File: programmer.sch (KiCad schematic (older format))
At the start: 2 parts

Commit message: FPGA change and new project file
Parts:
- removed U?: XC6SLX9-2TQG144I, symbol FPGA_Xilinx_Spartan6:XC6SLX4-TQG144
- added U?: XC7S6-1FTGB196C, Xilinx-XC7S6-1FTGB196C-0-0-*, symbol sdr:XC7S6-1FTGB196C
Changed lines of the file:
@@
 $EndDescr
-$Comp
-L FPGA_Xilinx_Spartan6:XC6SLX4-TQG144 U?
-U 3 1 60050A88
-P 7800 5150
-F 0 "U?" H 6520 5241 50  0000 R CNN
-F 1 "XC6SLX9-2TQG144I" H 6520 5150 50  0000 R CNN
-F 2 "" H 7800 5150 50  0001 C CNN
-F 3 "http://www.farnell.com/datasheets/1763510.pdf" H 6520 5059 50  0000 R CNN
-	3    7800 5150
-	-1   0    0    -1
-$EndComp
 $Comp
 L Interface_USB:FT2232HL U?
@@
 	1    0    0    -1
 $EndComp
+$Comp
+L sdr:XC7S6-1FTGB196C U?
+U 1 1 6004AE97
+P 7450 4000
+F 0 "U?" H 8550 4265 50  0000 C CNN
+F 1 "XC7S6-1FTGB196C" H 8550 4174 50  0000 C CNN
+F 2 "Xilinx-XC7S6-1FTGB196C-0-0-*" H 7450 4400 50  0001 L CNN
+F 3 "https://www.xilinx.com/support/documentation/data_sheets/ds189-spartan-7-data-sheet.pdf" H 7450 4500 50  0001 L CNN
+F 4 "180Kbits" H 7450 4600 50  0001 L CNN "RAM size"
+F 5 "No" H 7450 4700 50  0001 L CNN "automotive"
+F 6 "IC" H 7450 4800 50  0001 L CNN "category"
+F 7 "Integrated Circuits (ICs)" H 7450 4900 50  0001 L CNN "device class L1"
+F 8 "Embedded Processors and Controllers" H 7450 5000 50  0001 L CNN "device class L2"
+F 9 "FPGAs - Field Programmable Gate Arrays" H 7450 5100 50  0001 L CNN "device class L3"
+F 10 "XC7S6-1FTGB196C" H 7450 5200 50  0001 L CNN "digikey description"
+F 11 "122-2240-ND" H 7450 5300 50  0001 L CNN "digikey part number"
+F 12 "https://www.xilinx.com/support/documentation/user_guides/ug475_7Series_Pkg_Pinout.pdf" H 7450 5400 50  0001 L CNN "footprint url"
+F 13 "200MHz" H 7450 5500 50  0001 L CNN "frequency"
+F 14 "1.55mm" H 7450 5600 50  0001 L CNN "height"
+F 15 "BGA196C100P14X14_1500X1500X146" H 7450 5700 50  0001 L CNN "ipc land pattern name"
+F 16 "Yes" H 7450 5800 50  0001 L CNN "lead free"
+F 17 "d5f555df3775b1ed" H 7450 5900 50  0001 L CNN "library id"
+F 18 "Xilinx" H 7450 6000 50  0001 L CNN "manufacturer"
+F 19 "+85°C" H 7450 6100 50  0001 L CNN "max junction temp"
+F 20 "3.465V" H 7450 6200 50  0001 L CNN "max supply voltage"
+F 21 "0.95V" H 7450 6300 50  0001 L CNN "min supply voltage"
+F 22 "100" H 7450 6400 50  0001 L CNN "number of I/Os"
+F 23 "938" H 7450 6500 50  0001 L CNN "number of logic blocks"
+F 24 "6000" H 7450 6600 50  0001 L CNN "number of logic elements cells"
+F 25 "FTGB196" H 7450 6700 50  0001 L CNN "package"
+F 26 "0.13ns" H 7450 6800 50  0001 L CNN "propagation delay"
+F 27 "Yes" H 7450 6900 50  0001 L CNN "rohs"
+F 28 "1" H 7450 7000 50  0001 L CNN "speed grade"
+F 29 "0.3mm" H 7450 7100 50  0001 L CNN "standoff height"
+F 30 "+85°C" H 7450 7200 50  0001 L CNN "temperature range high"
+F 31 "0°C" H 7450 7300 50  0001 L CNN "temperature range low"
+	1    7450 4000
+	1    0    0    -1
+$EndComp

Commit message: finish up power supply
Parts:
- U?: symbol Interface_USB:FT2232HL -> open_hf_sdr-rescue:FT2232HL-Interface_USB
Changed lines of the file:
@@
 $EndDescr
 $Comp
-L Interface_USB:FT2232HL U?
+L open_hf_sdr-rescue:FT2232HL-Interface_USB U?
 U 1 1 60055DFE
 P 3500 3800

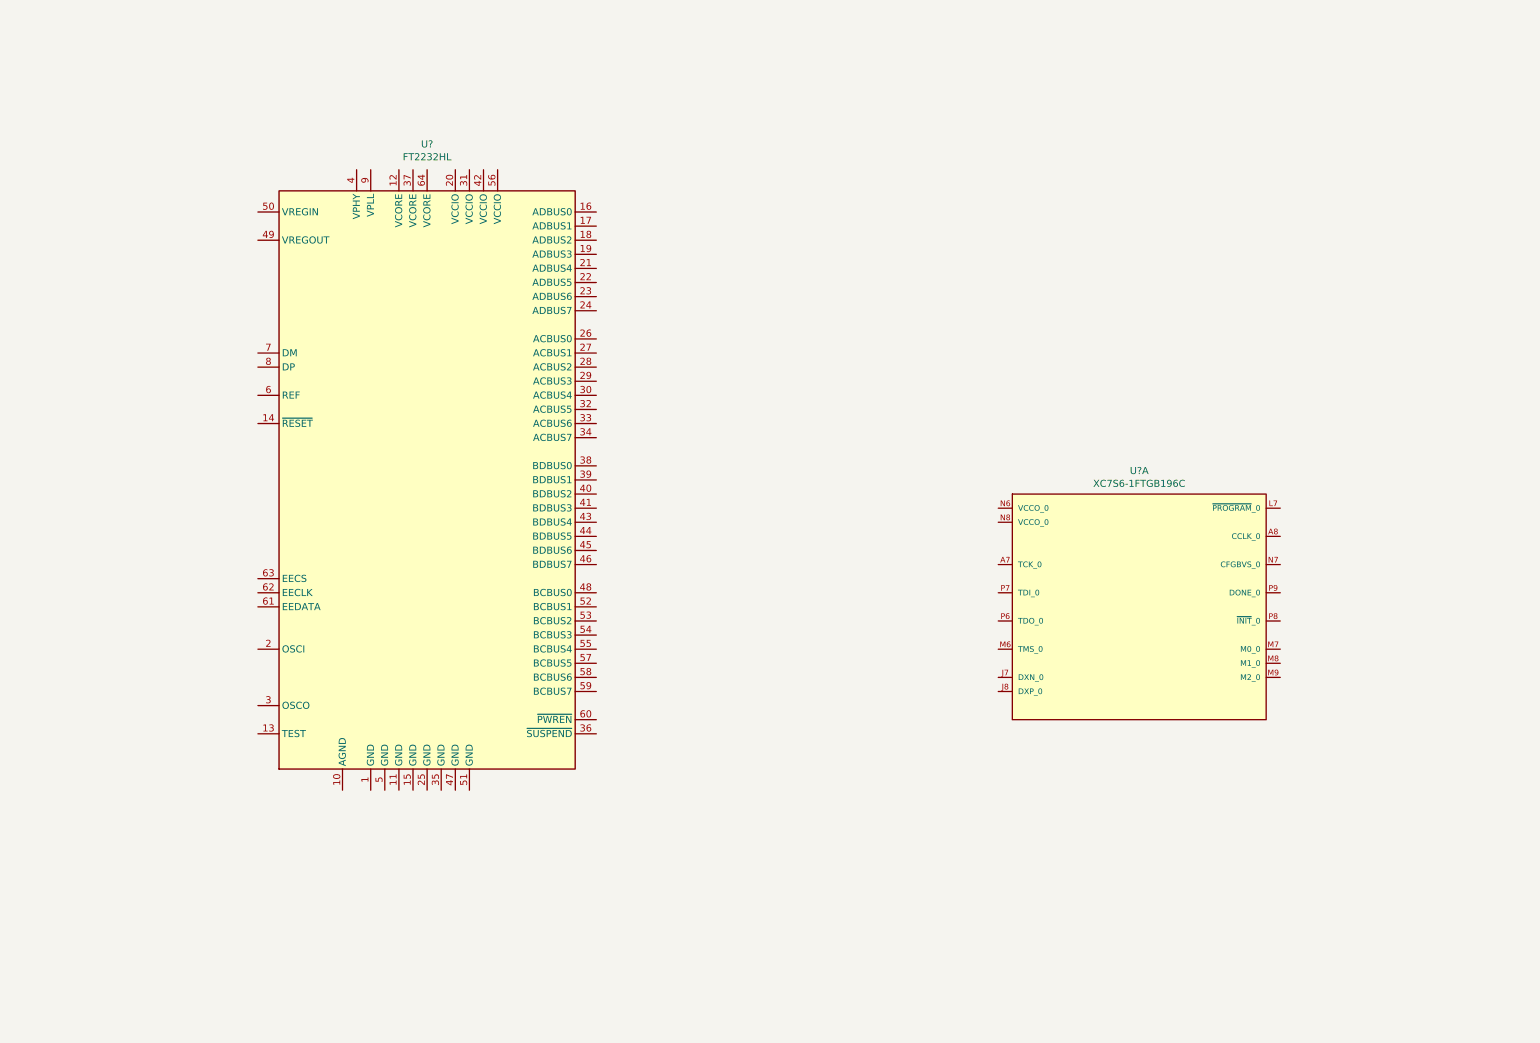
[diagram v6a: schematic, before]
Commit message: Progress in programmer sheet
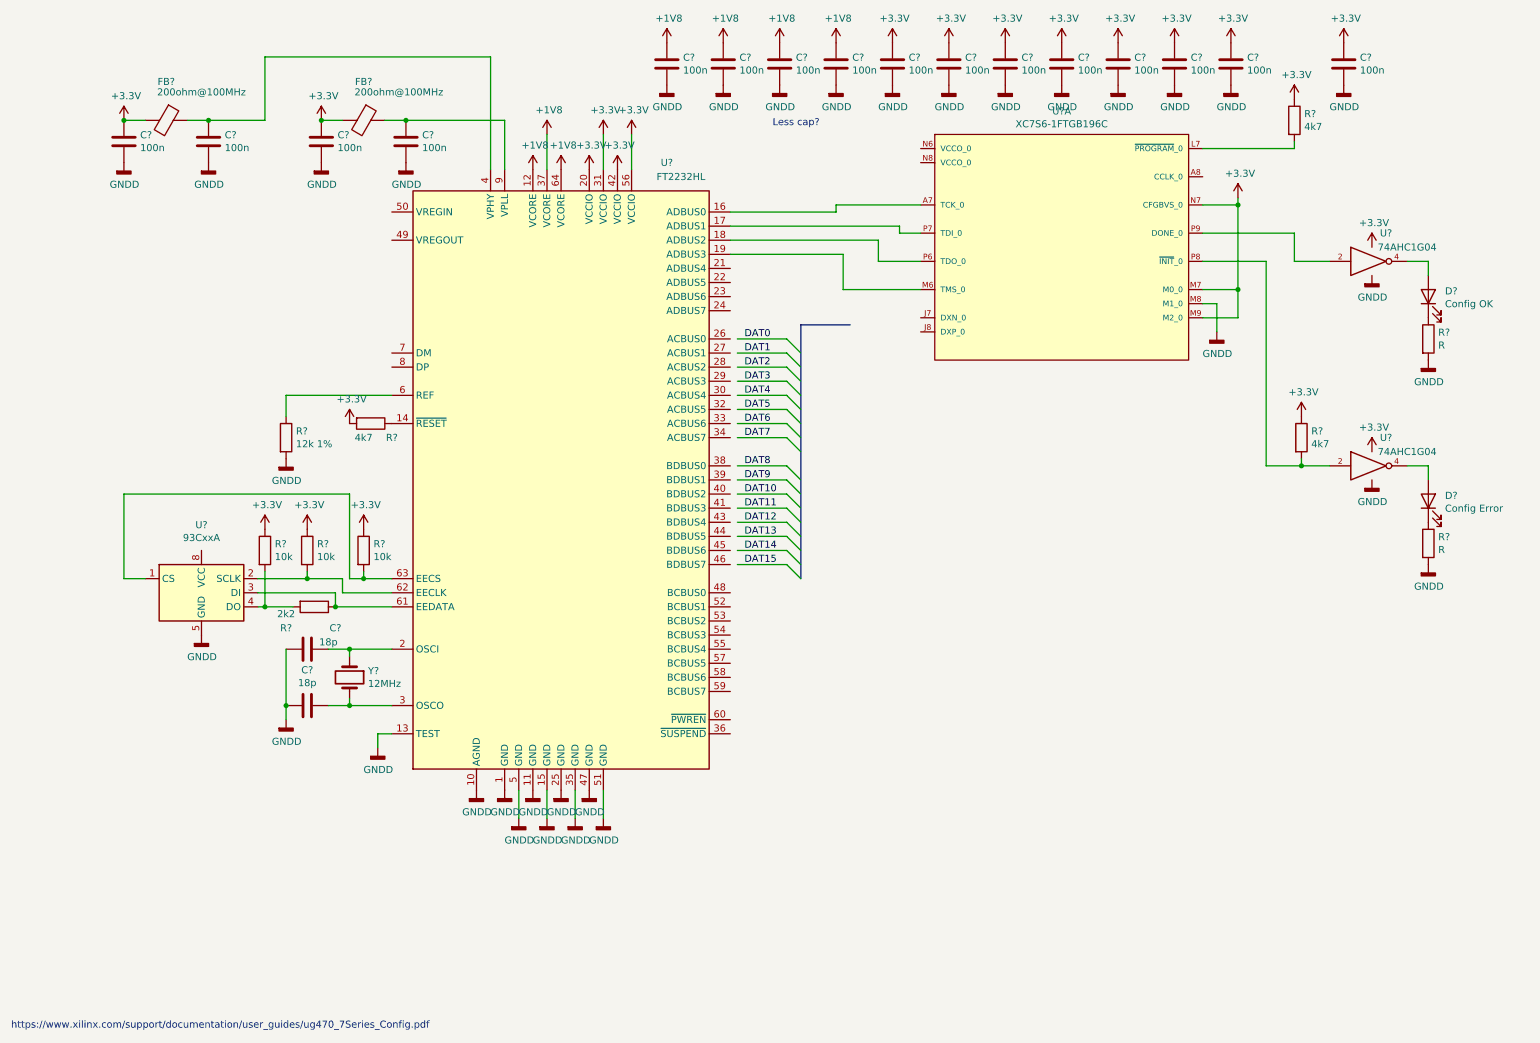
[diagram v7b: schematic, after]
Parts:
- added C? (x2): 18p, symbol Device:C
- added C? (x16): 100n, symbol Device:C
- added D?: Config Error, symbol Device:LED
- added D?: Config OK, symbol Device:LED
- added FB? (x2): 200ohm@100MHz, symbol Device:Ferrite_Bead
- added R? (x3): 4k7, symbol Device:R
- added R? (x2): R, symbol Device:R
- added R?: 12k 1%, symbol Device:R
- added R?: 2k2, symbol Device:R
- added R? (x3): 10k, symbol Device:R
- added U? (x2): 74AHC1G04, symbol 74xGxx:74AHC1G04
- added U?: 93CxxA, symbol Memory_EEPROM:93CxxA
- added Y?: 12MHz, symbol Device:Crystal
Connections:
- net labels added: +1V8, +3.3V, DAT0, DAT1, DAT10, DAT11, DAT12, DAT13, DAT14, DAT15, DAT2, DAT3, DAT4, DAT5, DAT6, DAT7, DAT8, DAT9, GNDD
- wire segments 0 -> 97
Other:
- note added: "Less cap?"
- note added: "https://www.xilinx.com/support/documentation/user_guides/ug470_7Series_Config.pdf"
- moved on the sheet: U?, U?A

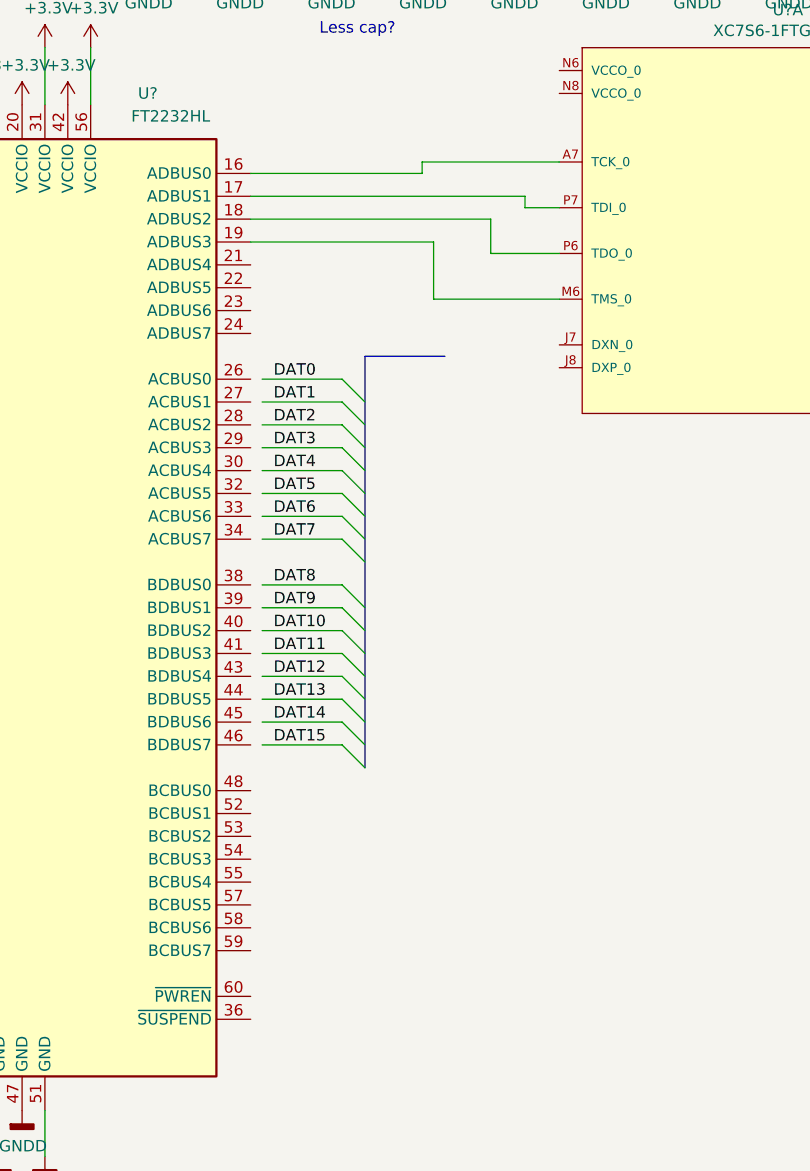
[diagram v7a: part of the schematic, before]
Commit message: Add USB-FPGA bus labels
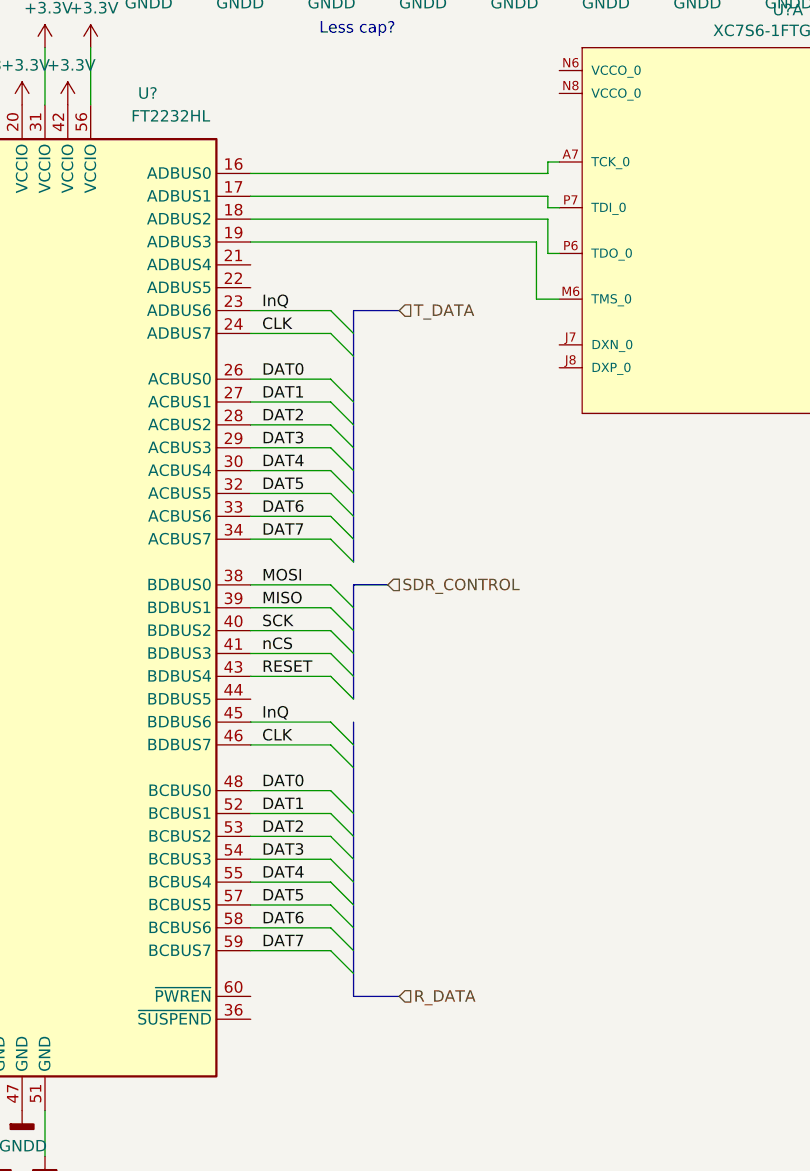
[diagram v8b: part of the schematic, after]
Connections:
- net labels added: CLK, InQ, MISO, MOSI, RESET, R_DATA, SCK, SDR_CONTROL, T_DATA, nCS
- net labels removed: DAT10, DAT11, DAT12, DAT13, DAT14, DAT15, DAT8, DAT9
- wire segments 97 -> 106
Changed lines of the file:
@@
 $EndComp
 Wire Wire Line
-	7000 1850 6400 1850
-Wire Wire Line
-	6400 1850 6400 1900
-Wire Wire Line
-	6400 1900 5650 1900
-Wire Wire Line
-	5650 2000 6850 2000
-Wire Wire Line
-	6850 2000 6850 2050
-Wire Wire Line
-	6850 2050 7000 2050
-Wire Wire Line
-	5650 2100 6700 2100
-Wire Wire Line
-	6700 2100 6700 2250
-Wire Wire Line
-	6700 2250 7000 2250
-Wire Wire Line
-	5650 2200 6450 2200
-Wire Wire Line
-	6450 2200 6450 2450
-Wire Wire Line
-	6450 2450 7000 2450
+	7000 1850 6950 1850
+Wire Wire Line
+	6950 1850 6950 1900
+Wire Wire Line
+	6950 1900 5650 1900
+Wire Wire Line
+	5650 2000 6950 2000
+Wire Wire Line
+	6950 2000 6950 2050
+Wire Wire Line
+	6950 2050 7000 2050
+Wire Wire Line
+	5650 2100 6950 2100
+Wire Wire Line
+	6950 2100 6950 2250
+Wire Wire Line
+	6950 2250 7000 2250
+Wire Wire Line
+	5650 2200 6900 2200
+Wire Wire Line
+	6900 2200 6900 2450
+Wire Wire Line
+	6900 2450 7000 2450
 $Comp
 L power:+3.3V #PWR?
@@
 	9650 2250 9900 2250
 Entry Wire Line
-	6050 2800 6150 2900
-Entry Wire Line
-	6050 2900 6150 3000
-Entry Wire Line
-	6050 3000 6150 3100
-Entry Wire Line
-	6050 3100 6150 3200
-Entry Wire Line
-	6050 3200 6150 3300
-Entry Wire Line
-	6050 3300 6150 3400
-Entry Wire Line
-	6050 3400 6150 3500
-Entry Wire Line
-	6050 3500 6150 3600
-Entry Wire Line
-	6050 3700 6150 3800
-Entry Wire Line
-	6050 3800 6150 3900
-Entry Wire Line
-	6050 3900 6150 4000
-Entry Wire Line
-	6050 4000 6150 4100
-Entry Wire Line
-	6050 4100 6150 4200
-Entry Wire Line
-	6050 4200 6150 4300
-Entry Wire Line
-	6050 4300 6150 4400
-Entry Wire Line
-	6050 4400 6150 4500
-Wire Wire Line
-	5700 2800 6050 2800
-Wire Wire Line
-	5700 2900 6050 2900
-Wire Wire Line
-	5700 3000 6050 3000
-Wire Wire Line
-	5700 3100 6050 3100
-Wire Wire Line
-	5700 3200 6050 3200
-Wire Wire Line
-	5700 3300 6050 3300
-Wire Wire Line
-	5700 3400 6050 3400
-Wire Wire Line
-	5700 3500 6050 3500
-Wire Wire Line
-	5700 3700 6050 3700
-Wire Wire Line
-	5700 3800 6050 3800
-Wire Wire Line
-	5700 3900 6050 3900
-Wire Wire Line
-	5700 4000 6050 4000
-Wire Wire Line
-	5700 4100 6050 4100
-Wire Wire Line
-	5700 4200 6050 4200
-Wire Wire Line
-	5700 4300 6050 4300
-Wire Wire Line
-	5700 4400 6050 4400
-Text Label 5750 2800 0    50   ~ 0
+	6000 2800 6100 2900
+Entry Wire Line
+	6000 2900 6100 3000
+Entry Wire Line
+	6000 3000 6100 3100
+Entry Wire Line
+	6000 3100 6100 3200
+Entry Wire Line
+	6000 3200 6100 3300
+Entry Wire Line
+	6000 3300 6100 3400
+Entry Wire Line
+	6000 3400 6100 3500
+Entry Wire Line
+	6000 3500 6100 3600
+Wire Wire Line
+	5650 2800 6000 2800
+Wire Wire Line
+	5650 2900 6000 2900
+Wire Wire Line
+	5650 3000 6000 3000
+Wire Wire Line
+	5650 3100 6000 3100
+Wire Wire Line
+	5650 3200 6000 3200
+Wire Wire Line
+	5650 3300 6000 3300
+Wire Wire Line
+	5650 3400 6000 3400
+Wire Wire Line
+	5650 3500 6000 3500
+Text Label 5700 2800 0    50   ~ 0
 DAT0
-Text Label 5750 2900 0    50   ~ 0
+Text Label 5700 2900 0    50   ~ 0
 DAT1
-Text Label 5750 3000 0    50   ~ 0
+Text Label 5700 3000 0    50   ~ 0
 DAT2
-Text Label 5750 3100 0    50   ~ 0
+Text Label 5700 3100 0    50   ~ 0
 DAT3
-Text Label 5750 3200 0    50   ~ 0
+Text Label 5700 3200 0    50   ~ 0
 DAT4
-Text Label 5750 3300 0    50   ~ 0
+Text Label 5700 3300 0    50   ~ 0
 DAT5
-Text Label 5750 3400 0    50   ~ 0
+Text Label 5700 3400 0    50   ~ 0
 DAT6
-Text Label 5750 3500 0    50   ~ 0
+Text Label 5700 3500 0    50   ~ 0
 DAT7
-Text Label 5750 3700 0    50   ~ 0
-DAT8
-Text Label 5750 3800 0    50   ~ 0
-DAT9
-Text Label 5750 3900 0    50   ~ 0
-DAT10
-Text Label 5750 4000 0    50   ~ 0
-DAT11
-Text Label 5750 4100 0    50   ~ 0
-DAT12
-Text Label 5750 4200 0    50   ~ 0
-DAT13
-Text Label 5750 4300 0    50   ~ 0
-DAT14
-Text Label 5750 4400 0    50   ~ 0
-DAT15
-Wire Bus Line
-	6150 2700 6500 2700
 Wire Wire Line
 	9000 2250 9450 2250
@@
 Wire Wire Line
 	3050 4500 2950 4500
+Entry Wire Line
+	6000 3700 6100 3800
+Entry Wire Line
+	6000 3800 6100 3900
+Entry Wire Line
+	6000 3900 6100 4000
+Entry Wire Line
+	6000 4000 6100 4100
+Text Label 5700 3700 0    50   ~ 0
+MOSI
+Text Label 5700 3800 0    50   ~ 0
+MISO
+Text Label 5700 3900 0    50   ~ 0
+SCK
+Text Label 5700 4000 0    50   ~ 0
+nCS
 Wire Bus Line
-	6150 2700 6150 4500
+	6100 3700 6250 3700
+Text HLabel 6250 3700 2    50   Input ~ 0
+SDR_CONTROL
+Wire Wire Line
+	5650 2600 6000 2600
+Entry Wire Line
+	6000 2600 6100 2700
+Text Label 5700 2600 0    50   ~ 0
+CLK
+Wire Wire Line
+	5650 2500 6000 2500
+Entry Wire Line
+	6000 2500 6100 2600
+Text Label 5700 2500 0    50   ~ 0
+InQ
+Wire Bus Line
+	6100 2500 6300 2500
+Text HLabel 6300 2500 2    50   Input ~ 0
+T_DATA
+Entry Wire Line
+	6000 4600 6100 4700
+Entry Wire Line
+	6000 4700 6100 4800
+Entry Wire Line
+	6000 4800 6100 4900
+Entry Wire Line
+	6000 4900 6100 5000
+Entry Wire Line
+	6000 5000 6100 5100
+Entry Wire Line
+	6000 5100 6100 5200
+Entry Wire Line
+	6000 5200 6100 5300
+Entry Wire Line
+	6000 5300 6100 5400
+Wire Wire Line
+	5650 4600 6000 4600
+Wire Wire Line
+	5650 4700 6000 4700
+Wire Wire Line
+	5650 4800 6000 4800
+Wire Wire Line
+	5650 4900 6000 4900
+Wire Wire Line
+	5650 5000 6000 5000
+Wire Wire Line
+	5650 5100 6000 5100
+Wire Wire Line
+	5650 5200 6000 5200
+Wire Wire Line
+	5650 5300 6000 5300
+Text Label 5700 4600 0    50   ~ 0
+DAT0
+Text Label 5700 4700 0    50   ~ 0
+DAT1
+Text Label 5700 4800 0    50   ~ 0
+DAT2
+Text Label 5700 4900 0    50   ~ 0
+DAT3
+Text Label 5700 5000 0    50   ~ 0
+DAT4
+Text Label 5700 5100 0    50   ~ 0
+DAT5
+Text Label 5700 5200 0    50   ~ 0
+DAT6
+Text Label 5700 5300 0    50   ~ 0
+DAT7
+Wire Wire Line
+	5650 4400 6000 4400
+Entry Wire Line
+	6000 4400 6100 4500
+Text Label 5700 4400 0    50   ~ 0
+CLK
+Wire Wire Line
+	5650 4300 6000 4300
+Entry Wire Line
+	6000 4300 6100 4400
+Text Label 5700 4300 0    50   ~ 0
+InQ
+Wire Bus Line
+	6100 5500 6300 5500
+Text HLabel 6300 5500 2    50   Input ~ 0
+R_DATA
+Wire Wire Line
+	5650 3700 6000 3700
+Wire Wire Line
+	5650 3800 6000 3800
+Wire Wire Line
+	5650 3900 6000 3900
+Wire Wire Line
+	5650 4000 6000 4000
+Wire Wire Line
+	5650 4100 6000 4100
+Text Label 5700 4100 0    50   ~ 0
+RESET
+Entry Wire Line
+	6000 4100 6100 4200
+Wire Bus Line
+	6100 3700 6100 4200
+Wire Bus Line
+	6100 2500 6100 3600
+Wire Bus Line
+	6100 4300 6100 5500
 $EndSCHEMATC
